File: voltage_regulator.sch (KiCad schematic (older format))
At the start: 3 parts, among them U1 AP2204R-3.3TRG1

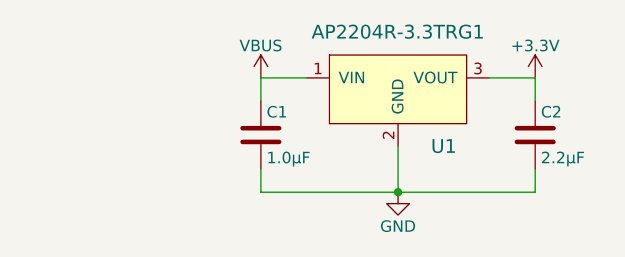
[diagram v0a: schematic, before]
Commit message: 4-layer board with smaller components
This is a major change!  Almost all the components have changed to
smaller versions, with 0603 and 0402 passives and a QFN microcontroller.
The board now has four layers, with internal layers used for VBUS and
GND.  The board now measures a mere 25×30 mm!  The SWD header and Boot
switch footprints have been moved to the bottom to help with this
shrinkage.  Two test points were added to the bottom as well to make it
possible to power the board without using the USB connector.  The
mounting holes are now slightly smaller (better sized for M3), and only
17 mm apart instead of the old 18 mm.

To sum up, everything is smaller and that's almost entirely a good
thing, except now it's not really possible to build one by hand.
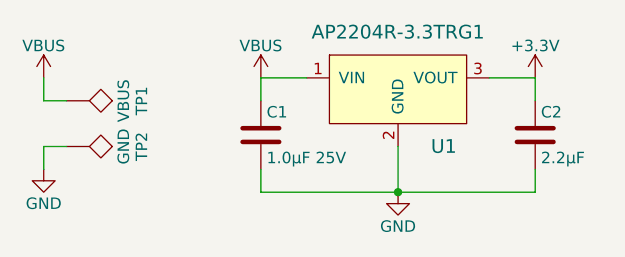
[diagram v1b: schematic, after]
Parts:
- added TP1: VBUS, Measurement_Points:Measurement_Point_Round-SMD-Pad_Small, symbol TEST
- added TP2: GND, Measurement_Points:Measurement_Point_Round-SMD-Pad_Small, symbol TEST
- C1: value 1.0μF -> 1.0μF 25V; footprint Capacitors_SMD:C_0805 -> Capacitors_SMD:C_0603
- C2: footprint Capacitors_SMD:C_0805 -> Capacitors_SMD:C_0603
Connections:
- net GND: now also TP2.1
- net VBUS: now also TP1.1
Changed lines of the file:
@@
 F 0 "C2" H 6675 3850 50  0000 L CNN
 F 1 "2.2μF" H 6675 3650 50  0000 L CNN
-F 2 "Capacitors_SMD:C_0805" H 6688 3600 50  0001 C CNN
+F 2 "Capacitors_SMD:C_0603" H 6688 3600 50  0001 C CNN
 F 3 "" H 6650 3750 50  0000 C CNN
 	1    6650 3750
@@
 P 5450 3750
 F 0 "C1" H 5475 3850 50  0000 L CNN
-F 1 "1.0μF" H 5475 3650 50  0000 L CNN
-F 2 "Capacitors_SMD:C_0805" H 5488 3600 50  0001 C CNN
+F 1 "1.0μF 25V" H 5475 3650 50  0000 L CNN
+F 2 "Capacitors_SMD:C_0603" H 5488 3600 50  0001 C CNN
 F 3 "" H 5450 3750 50  0000 C CNN
 	1    5450 3750
@@
 	1    0    0    -1
 $EndComp
+$Comp
+L VBUS #PWR06
+U 1 1 58FBCEC4
+P 4500 3500
+F 0 "#PWR06" H 4500 3350 50  0001 C CNN
+F 1 "VBUS" H 4500 3640 50  0000 C CNN
+F 2 "" H 4500 3500 50  0000 C CNN
+F 3 "" H 4500 3500 50  0000 C CNN
+	1    4500 3500
+	1    0    0    -1
+$EndComp
+$Comp
+L GND #PWR07
+U 1 1 58FBCEDB
+P 4500 3900
+F 0 "#PWR07" H 4500 3650 50  0001 C CNN
+F 1 "GND" H 4500 3750 50  0000 C CNN
+F 2 "" H 4500 3900 50  0000 C CNN
+F 3 "" H 4500 3900 50  0000 C CNN
+	1    4500 3900
+	1    0    0    -1
+$EndComp
+$Comp
+L TEST TP1
+U 1 1 58FBCF4C
+P 4600 3600
+F 0 "TP1" H 4600 3900 50  0000 C BNN
+F 1 "VBUS" H 4600 3850 50  0000 C CNN
+F 2 "Measurement_Points:Measurement_Point_Round-SMD-Pad_Small" H 4600 3600 50  0001 C CNN
+F 3 "" H 4600 3600 50  0001 C CNN
+	1    4600 3600
+	0    1    1    0
+$EndComp
+$Comp
+L TEST TP2
+U 1 1 58FBD023
+P 4600 3800
+F 0 "TP2" H 4600 4100 50  0000 C BNN
+F 1 "GND" H 4600 4050 50  0000 C CNN
+F 2 "Measurement_Points:Measurement_Point_Round-SMD-Pad_Small" H 4600 3800 50  0001 C CNN
+F 3 "" H 4600 3800 50  0001 C CNN
+	1    4600 3800
+	0    1    1    0
+$EndComp
+Wire Wire Line
+	4600 3600 4500 3600
+Wire Wire Line
+	4500 3600 4500 3500
+Wire Wire Line
+	4600 3800 4500 3800
+Wire Wire Line
+	4500 3800 4500 3900
 $EndSCHEMATC
